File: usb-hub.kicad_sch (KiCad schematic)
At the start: 1 part, among them U1 USB2514B-I_M2

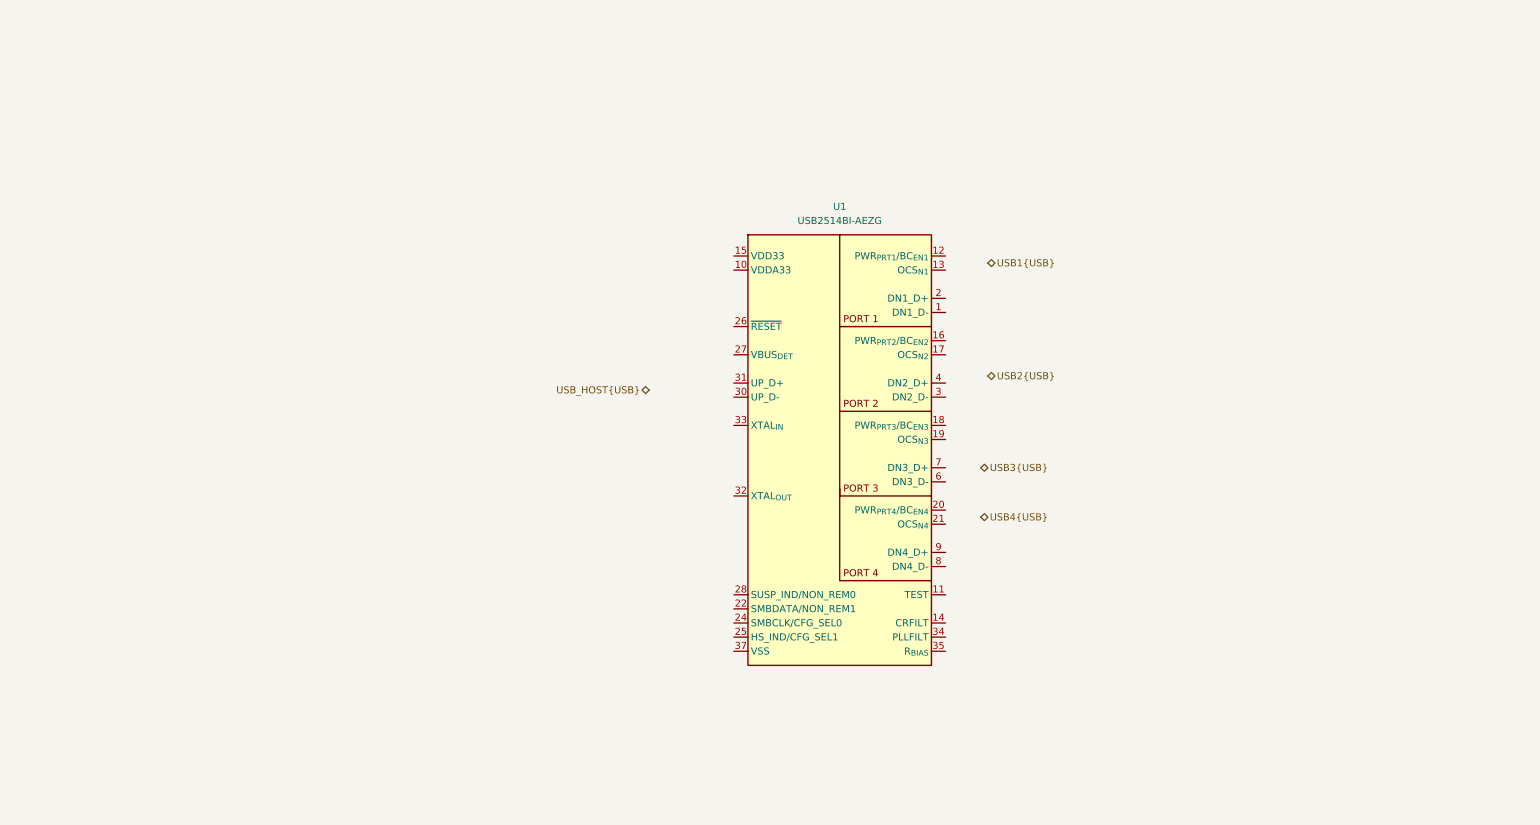
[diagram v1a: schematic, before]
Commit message: Add USB Hub, start selecting strap options
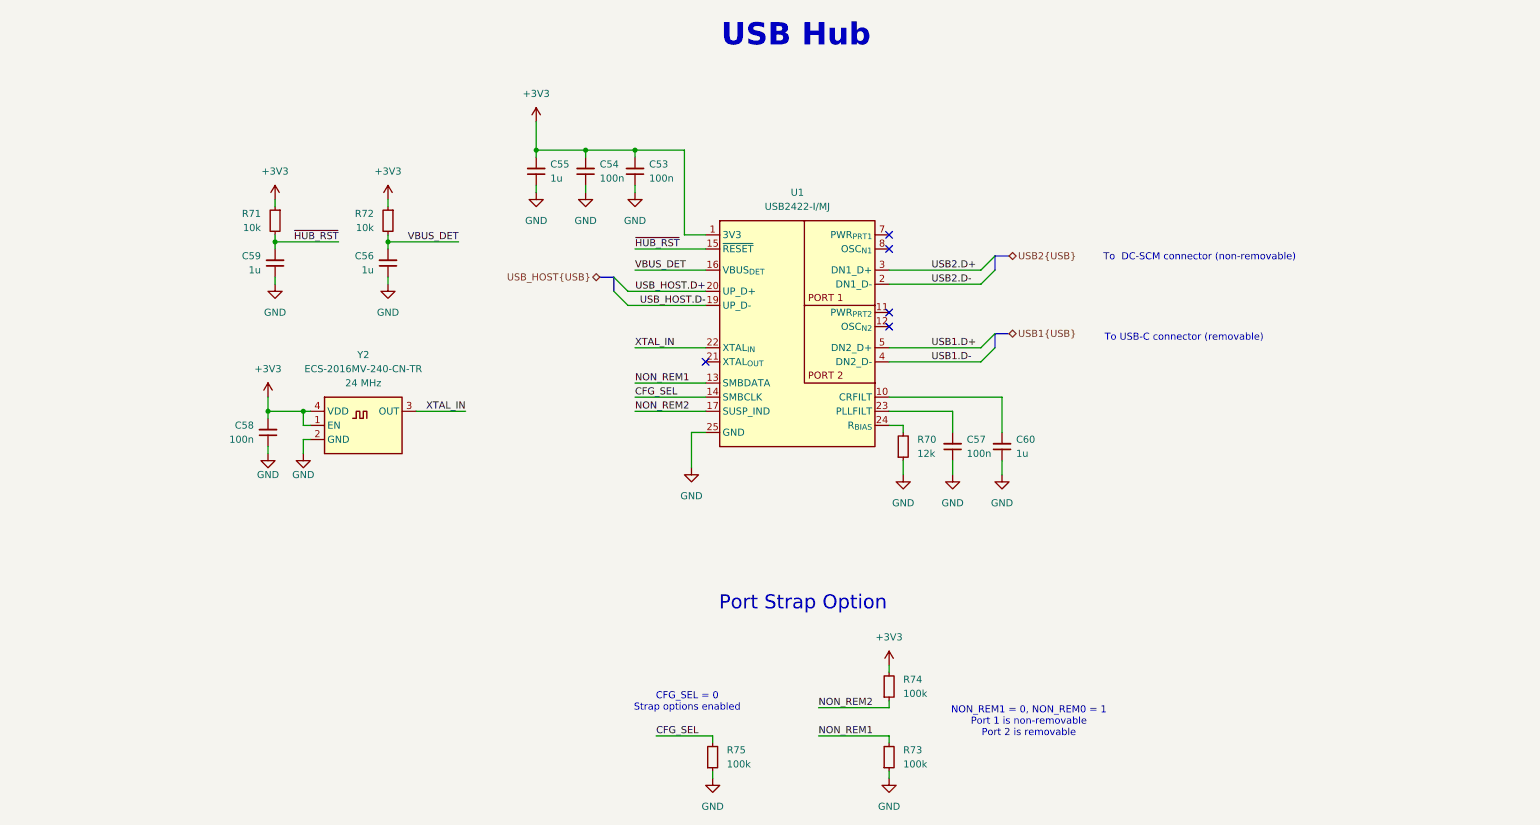
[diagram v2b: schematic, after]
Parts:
- removed U1: USB2514B-I_M2, antmicro-footprints:QFN-36-1EP_6x6mm_P0.5mm_EP3.7x3.7mm, symbol antmicroInterfaceControllers:USB2514B-I_M2
- added C53, C54, C57, C58: C_100n_0402, antmicro-footprints:C_0402_1005Metric, symbol Capacitors0402:C_100n_0402
- added C55, C56, C59, C60: C_1u_16V_0402, antmicro-footprints:C_0402_1005Metric, symbol Capacitors0402:C_1u_16V_0402
- added R70: R_12k_0402, antmicro-footprints:R_0402_1005Metric, symbol Resistors0402:R_12k_0402
- added R71, R72: R_10k_0402, antmicro-footprints:R_0402_1005Metric, symbol Resistors0402:R_10k_0402
- added R73, R74, R75: R_100k_0402, antmicro-footprints:R_0402_1005Metric, symbol Resistors0402:R_100k_0402
- added U1: USB2422-I_MJ, antmicro-footprints:QFN-24-1EP_4x4mm_P0.5mm_EP2.6x2.6mm, symbol InterfaceControllers:USB2422-I_MJ
- added Y2: Oscillator_24MHz_ESC_2016MV, antmicro-footprints:Oscillator_SMD_ECS_2016MV_2x1.6x0.85mm, symbol Oscillators:Oscillator_24MHz_ESC_2016MV
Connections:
- new net: C60.2, U1.10 (CRFILT)
- new net: C57.2, U1.23 (PLLFILT)
- new net: R70.2, U1.24 (R_{BIAS})
- new net +3V3: C53.2, C54.2, C55.2, C58.2, R71.1, R72.1, R74.2, U1.1 (3V3), U1.18 (3V3), U1.9 (3V3), Y2.1 (EN), Y2.4 (VDD)
- new net CFG_SEL: R75.2, U1.14 (SMBCLK)
- new net GND: C53.1, C54.1, C55.1, C56.1, C57.1, C58.1, C59.1, C60.1, R70.1, R73.1, R75.1, U1.25 (GND), Y2.2 (GND)
- new net NON_REM1: R73.2, U1.13 (SMBDATA)
- new net NON_REM2: R74.1, U1.17 (SUSP_IND)
- new net USB1.D+: U1.5 (DN2_D+)
- new net USB1.D-: U1.4 (DN2_D-)
- new net USB2.D+: U1.3 (DN1_D+)
- new net USB2.D-: U1.2 (DN1_D-)
- new net USB_HOST.D+: U1.20 (UP_D+)
- new net USB_HOST.D-: U1.19 (UP_D-)
- new net VBUS_DET: C56.2, R72.2, U1.16 (VBUS_{DET})
- new net XTAL_IN: U1.22 (XTAL_{IN}), Y2.3 (OUT)
- new net ~{HUB_RST}: C59.2, R71.2, U1.15 (~{RESET})
- no-connect marks 0 -> 5
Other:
- note added: "CFG_SEL = 0 Strap options enabled"
- note added: "NON_REM1 = 0, NON_REM0 = 1 Port 1 is non-removable Port 2 is removable"
- note added: "Port Strap Option"
- note added: "To DC-SCM connector (non-removable)"
- note added: "To USB-C connector (removable)"
- note added: "USB Hub"

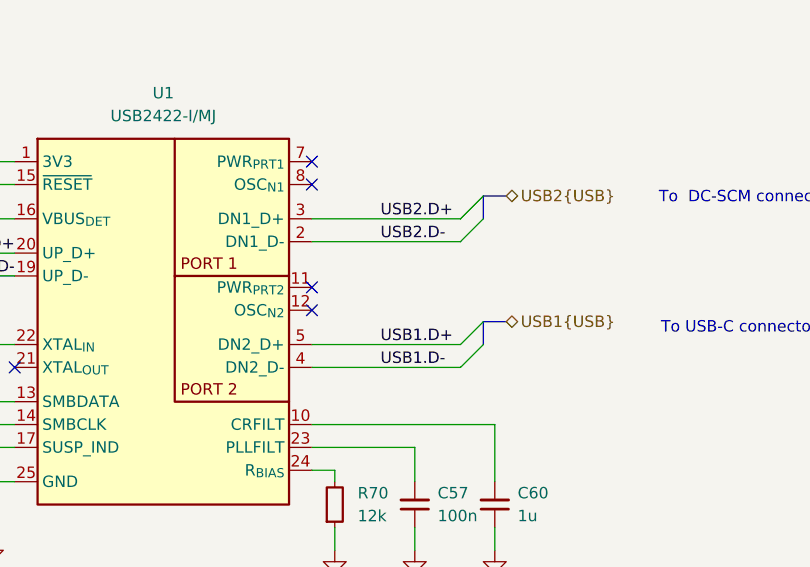
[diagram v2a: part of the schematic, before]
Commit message: Add CC controllers to USB0 and USB1
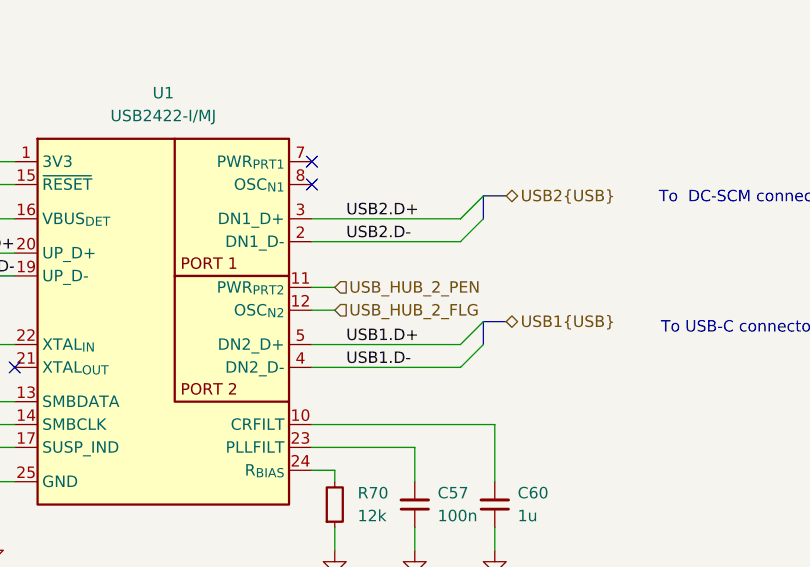
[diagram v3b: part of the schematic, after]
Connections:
- net USB_HUB_2_PEN: now reaches U1.11 (PWR_{PRT2})
- net USB_HUB_2_FLG: now reaches U1.12 (OSC_{N2})
- no-connect marks 5 -> 3
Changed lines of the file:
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@@
-	)
-	(no_connect
-		(at 199.39 114.3)
 	)
 	(no_connect
 		(at 199.39 100.33)
-	)
-	(no_connect
-		(at 199.39 116.84)
 	)
 	(no_connect
@@
 	(wire
 		(pts
+			(xy 199.39 116.84) (xy 201.93 116.84)
+		)
+		(stroke
+			(width 0)
+			(type default)
+		)
+	)
+	(wire
+		(pts
 			(xy 93.98 134.62) (xy 93.98 132.08)
 		)
@@
 		(pts
 			(xy 186.69 190.5) (xy 199.39 190.5)
+		)
+		(stroke
+			(width 0)
+			(type default)
+		)
+	)
+	(wire
+		(pts
+			(xy 199.39 114.3) (xy 201.93 114.3)
 		)
 		(stroke
@@
 	)
 	(label "USB1.D-"
-		(at 207.01 123.19 0)
+		(at 203.2 123.19 0)
 		(effects
 			(font
@@
 	)
 	(label "USB2.D+"
-		(at 207.01 106.68 0)
+		(at 203.2 106.68 0)
 		(effects
 			(font
@@
 	)
 	(label "USB2.D-"
-		(at 207.01 109.22 0)
+		(at 203.2 109.22 0)
 		(effects
 			(font
@@
 	)
 	(label "USB1.D+"
-		(at 207.01 120.65 0)
+		(at 203.2 120.65 0)
 		(effects
 			(font
@@
 		)
 	)
+	(hierarchical_label "USB_HUB_2_FLG"
+		(shape input)
+		(at 201.93 116.84 0)
+		(effects
+			(font
+				(size 1.27 1.27)
+			)
+			(justify left)
+		)
+	)
 	(hierarchical_label "USB1{USB}"
 		(shape bidirectional)
@@
 		(effects
 			(font
+				(size 1.27 1.27)
+			)
+			(justify left)
+		)
+	)
+	(hierarchical_label "USB_HUB_2_PEN"
+		(shape input)
+		(at 201.93 114.3 0)
+		(effects
+			(font

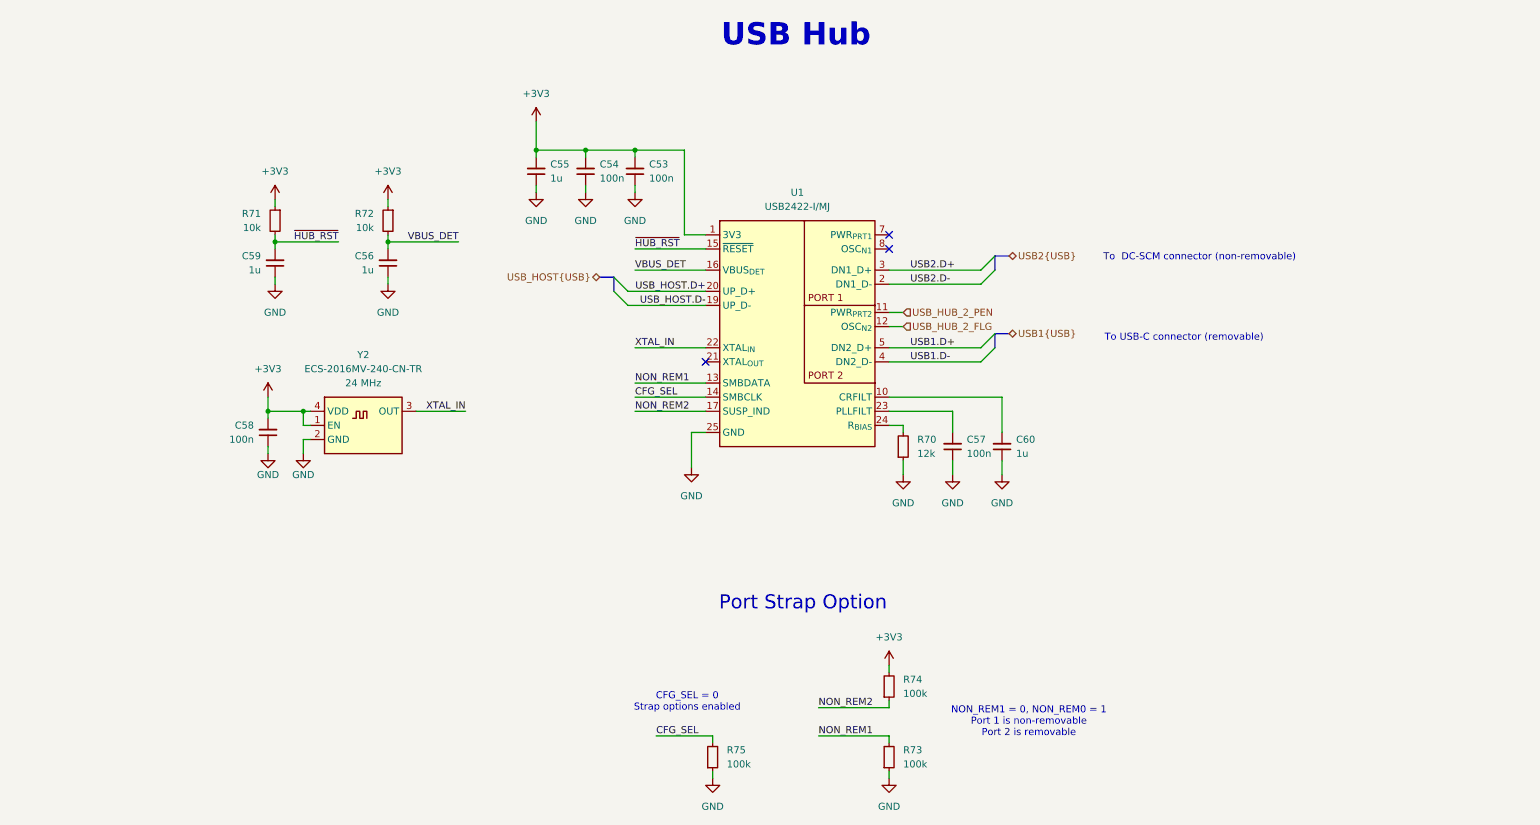
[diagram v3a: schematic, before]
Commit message: [#83336] Improved USB circuitry
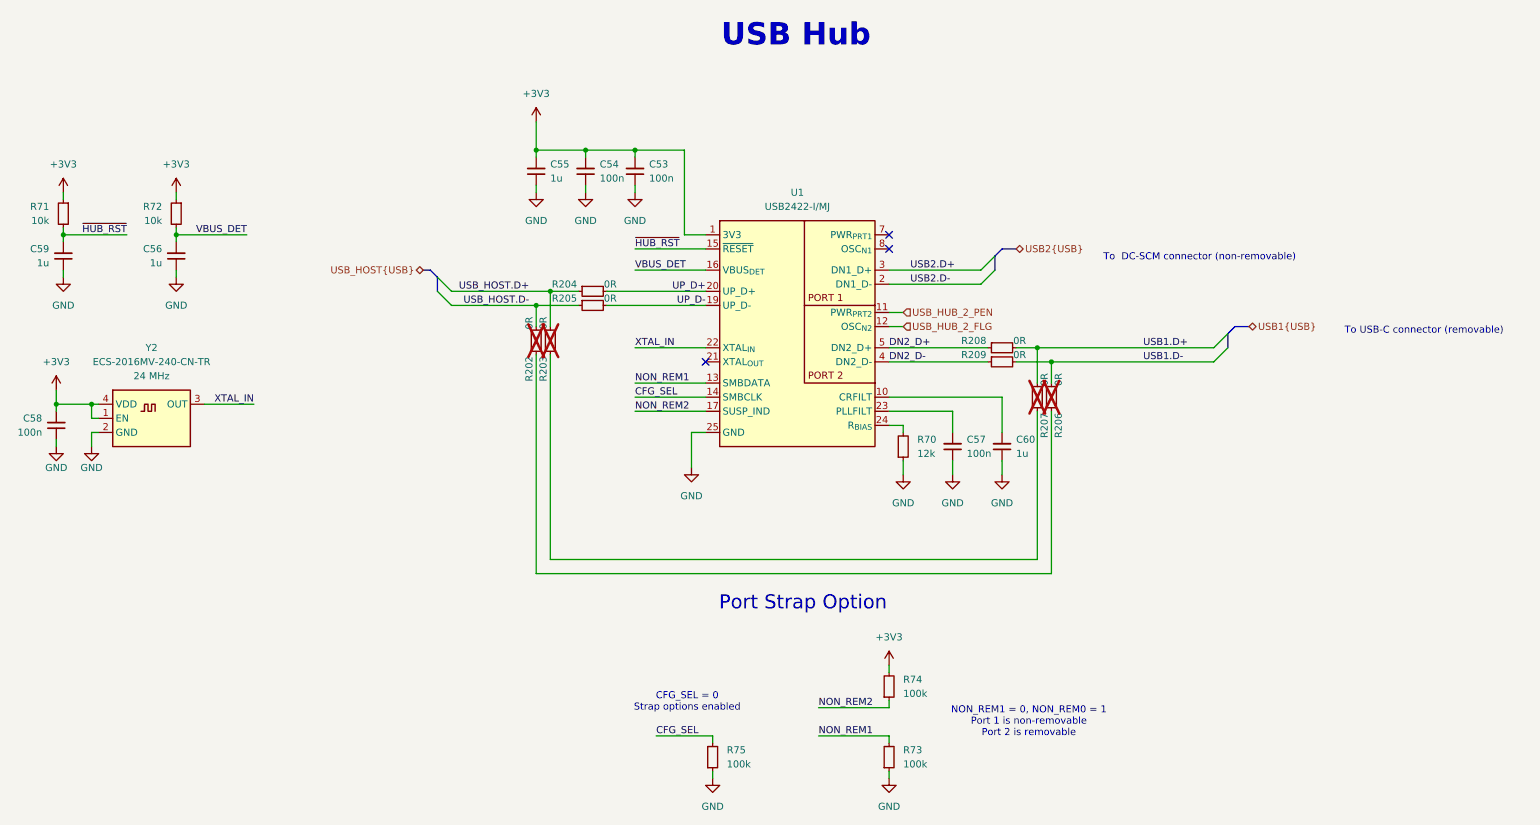
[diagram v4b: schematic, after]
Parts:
- added R202, R203, R204, R205, R206, R207, R208, R209: R_0R_0402, antmicro-footprints:R_0402_1005Metric, symbol antmicroResistors0402:R_0R_0402
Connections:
- net USB1.D+: now also R207.2, R208.2; no longer U1.5 (DN2_D+)
- net USB1.D-: now also R206.2, R209.2; no longer U1.4 (DN2_D-)
- net USB_HOST.D+: now also R203.2, R204.1; no longer U1.20 (UP_D+)
- net USB_HOST.D-: now also R202.2, R205.1; no longer U1.19 (UP_D-)
- new net: R202.1, R206.1
- new net: R203.1, R207.1
- new net DN2_D+: R208.1, U1.5 (DN2_D+)
- new net DN2_D-: R209.1, U1.4 (DN2_D-)
- new net UP_D+: R204.2, U1.20 (UP_D+)
- new net UP_D-: R205.2, U1.19 (UP_D-)
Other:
- moved on the sheet: C56, C58, C59, R71, R72, Y2

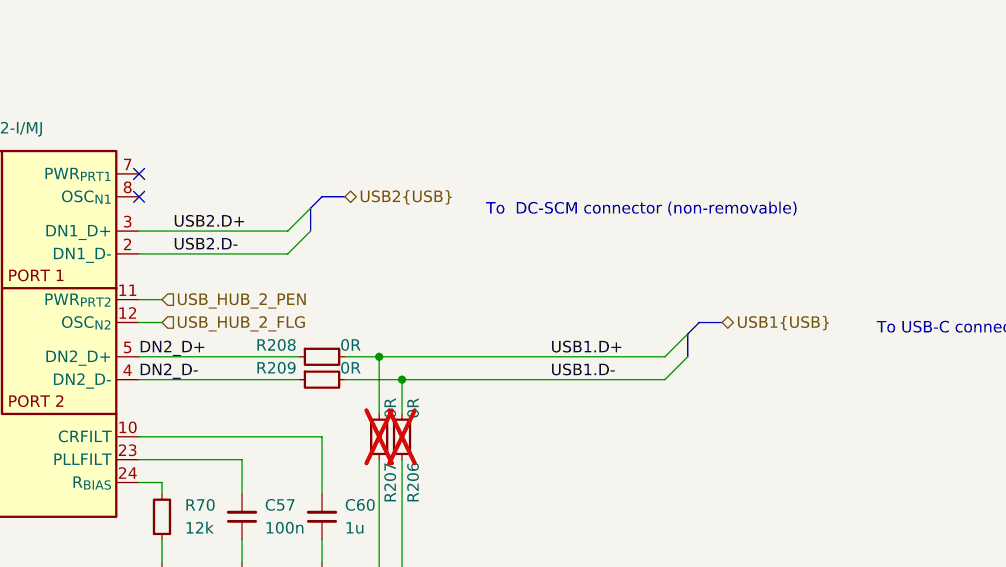
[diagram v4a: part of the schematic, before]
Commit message: [#83336] Small front panel interface fixes
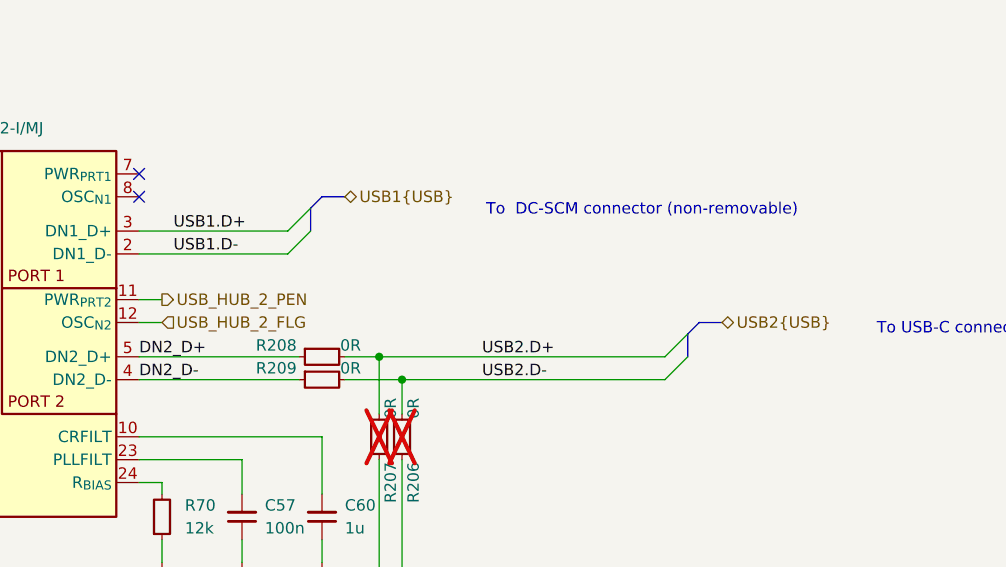
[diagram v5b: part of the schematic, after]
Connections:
- net USB1.D+: now also U1.3 (DN1_D+); no longer R207.2, R208.2
- net USB1.D-: now also U1.2 (DN1_D-); no longer R206.2, R209.2
- net USB2.D+: now also R207.2, R208.2; no longer U1.3 (DN1_D+)
- net USB2.D-: now also R206.2, R209.2; no longer U1.2 (DN1_D-)
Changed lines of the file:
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@@
 	)
 	(label "USB1.D-"
-		(at 245.11 123.19 0)
+		(at 203.2 109.22 0)
 		(effects
 			(font
@@
 	)
 	(label "USB2.D+"
-		(at 203.2 106.68 0)
+		(at 237.49 120.65 0)
 		(effects
 			(font
@@
 	)
 	(label "USB2.D-"
-		(at 203.2 109.22 0)
+		(at 237.49 123.19 0)
 		(effects
 			(font
@@
 	)
 	(label "USB1.D+"
-		(at 245.11 120.65 0)
+		(at 203.2 106.68 0)
 		(effects
 			(font
@@
 	(hierarchical_label "USB2{USB}"
 		(shape bidirectional)
-		(at 222.25 102.87 0)
+		(at 264.16 116.84 0)
 		(effects
 			(font
@@
 	(hierarchical_label "USB1{USB}"
 		(shape bidirectional)
-		(at 264.16 116.84 0)
+		(at 222.25 102.87 0)
 		(effects
 			(font
@@
 	)
 	(hierarchical_label "USB_HUB_2_PEN"
-		(shape input)
+		(shape output)
 		(at 201.93 114.3 0)
 		(effects

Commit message: [#83609] Reannotate board
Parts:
- renumbered C58 to C11, C59 to C12, C56 to C13, C55 to C14, C54 to C15, C53 to C16, C57 to C17, C60 to C18, R71 to R81, R72 to R82, R202 to R83, R203 to R84, R204 to R85, R205 to R86, R75 to R87, R74 to R88, R73 to R89, R70 to R90, R208 to R91, R209 to R92, R207 to R93, R206 to R94, U1 to U4, Y2 to Y1

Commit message: [#83736] WIP: Clear ERC
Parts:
- removed C11, C15, C16, C17: C_100n_0402, antmicro-footprints:C_0402_1005Metric, symbol Capacitors0402:C_100n_0402
- removed C12, C13, C14, C18: C_1u_16V_0402, antmicro-footprints:C_0402_1005Metric, symbol Capacitors0402:C_1u_16V_0402
- removed R87, R88, R89: R_100k_0402, antmicro-footprints:R_0402_1005Metric, symbol Resistors0402:R_100k_0402
- removed R90: R_12k_0402, antmicro-footprints:R_0402_1005Metric, symbol Resistors0402:R_12k_0402
- removed U4: USB2422-I_MJ, antmicro-footprints:QFN-24-1EP_4x4mm_P0.5mm_EP2.6x2.6mm, symbol InterfaceControllers:USB2422-I_MJ
- removed Y1: Oscillator_24MHz_ESC_2016MV, antmicro-footprints:Oscillator_SMD_ECS_2016MV_2x1.6x0.85mm, symbol Oscillators:Oscillator_24MHz_ESC_2016MV
- added C11, C14, C18, C183: C_100n_0402, antmicro-footprints:C_0402_1005Metric, symbol antmicroCapacitors0402:C_100n_0402
- added C12, C13, C17, C184: C_1u_0402, antmicro-footprints:C_0402_1005Metric, symbol antmicroCapacitors0402:C_1u_0402
- added R87, R88, R89: R_100k_0402, antmicro-footprints:R_0402_1005Metric, symbol antmicroResistors0402:R_100k_0402
- added R90: R_12k_0402, antmicro-footprints:R_0402_1005Metric, symbol antmicroResistors0402:R_12k_0402
- added U4: USB2422-I_MJ, antmicro-footprints:QFN-24-1EP_4x4mm_P0.5mm_EP2.6x2.6mm, symbol antmicroInterfaceControllers:USB2422-I_MJ
- added Y1: Oscillator_24MHz_ESC_2016MV, antmicro-footprints:Oscillator_SMD_ECS_2016MV_2x1.6x0.85mm, symbol antmicroOscillators:Oscillator_24MHz_ESC_2016MV
- R81, R82: symbol Resistors0402:R_10k_0402 -> antmicroResistors0402:R_10k_0402
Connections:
- net +3V3: now also C11.2, C14.2, C18.2, C184.2, R88.2, U4.1 (3V3), U4.18 (3V3), U4.9 (3V3), Y1.1 (EN), Y1.4 (VDD)
- net CFG_SEL: now also R87.2, U4.14 (SMBCLK)
- net DN2_D+: now also U4.5 (DN2_D+)
- net DN2_D-: now also U4.4 (DN2_D-)
- net GND: now also C11.1, C12.1, C13.1, C14.1, C17.1, C18.1, C183.1, C184.1, R87.1, R89.1, R90.1, U4.25 (GND), Y1.2 (GND)
- net NON_REM1: now also R89.2, U4.13 (SMBDATA)
- net NON_REM2: now also R88.1, U4.17 (SUSP_IND)
- net UP_D+: now also U4.20 (UP_D+)
- net UP_D-: now also U4.19 (UP_D-)
- net USB1.D+: now also U4.3 (DN1_D+)
- net USB1.D-: now also U4.2 (DN1_D-)
- net USB_HUB_2_FLG: now also U4.12 (OSC_{N2})
- net USB_HUB_2_PEN: now also U4.11 (PWR_{PRT2})
- net VBUS_DET: now also C13.2, U4.16 (VBUS_{DET})
- net XTAL_IN: now also U4.22 (XTAL_{IN}), Y1.3 (OUT)
- net ~{HUB_RST}: now also C12.2, U4.15 (~{RESET})
- new net: C17.2, U4.10 (CRFILT)
- new net: C183.2, U4.23 (PLLFILT)
- new net: R90.2, U4.24 (R_{BIAS})
